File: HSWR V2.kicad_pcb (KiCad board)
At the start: 4 copper layers, 152 x 139 mm, 156 parts, among them IC1 INA181, IC2 INA181, IC3 INA181, IC4 ADUM3054, IC5 ADuM4160, IC6 JW5052C, IC7 JW5052C, IC8 B1212S-2W, J1 IO, J10 SWD, J4 USB_B, J5 B+, J6 B-, J7 U, J8 V, J9 W, Q11 IXFK300N20X3, Q12 IXFK300N20X3, Q3 IXFK300N20X3, Q4 IXFK300N20X3, Q7 IXFK300N20X3, Q8 IXFK300N20X3, U1 STM32F405RGTx, U2 IRS2186, U3 IRS2186, U4 IRS2186, U5 AP1117-50, Y1 8MHz

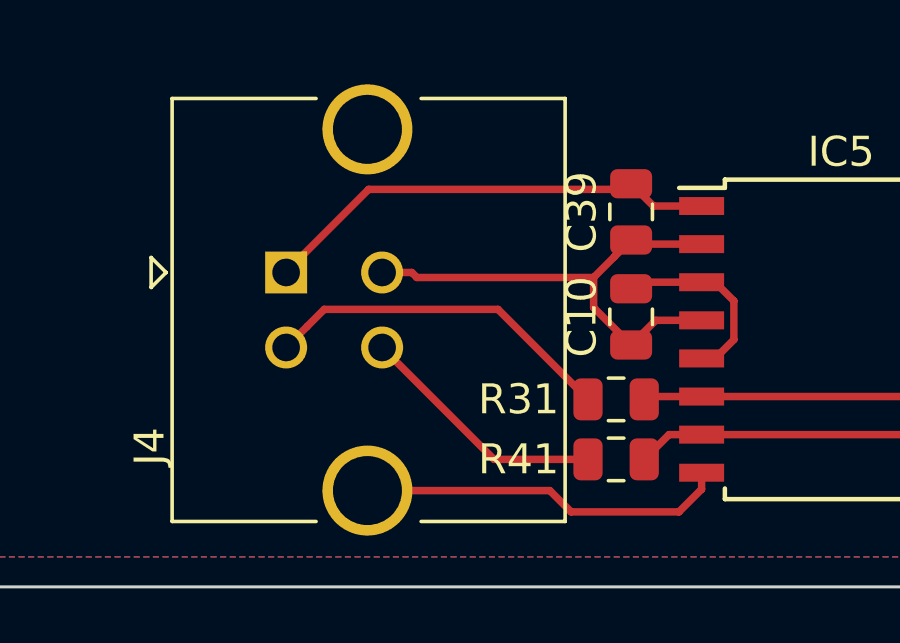
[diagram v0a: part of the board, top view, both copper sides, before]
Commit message: - corrected current filter resistors - adapted USB footprint - added 0.1% note to dc bus voltage divider
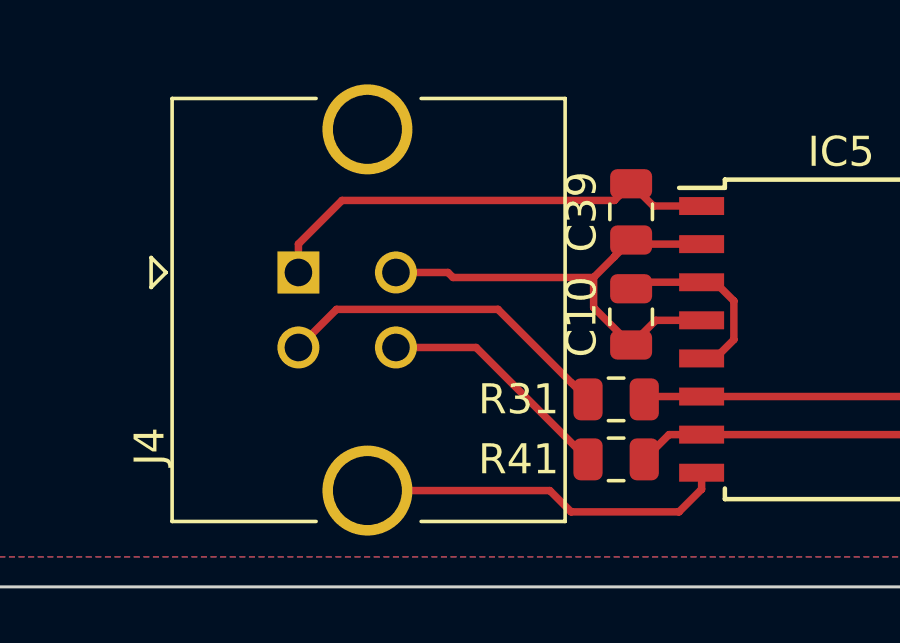
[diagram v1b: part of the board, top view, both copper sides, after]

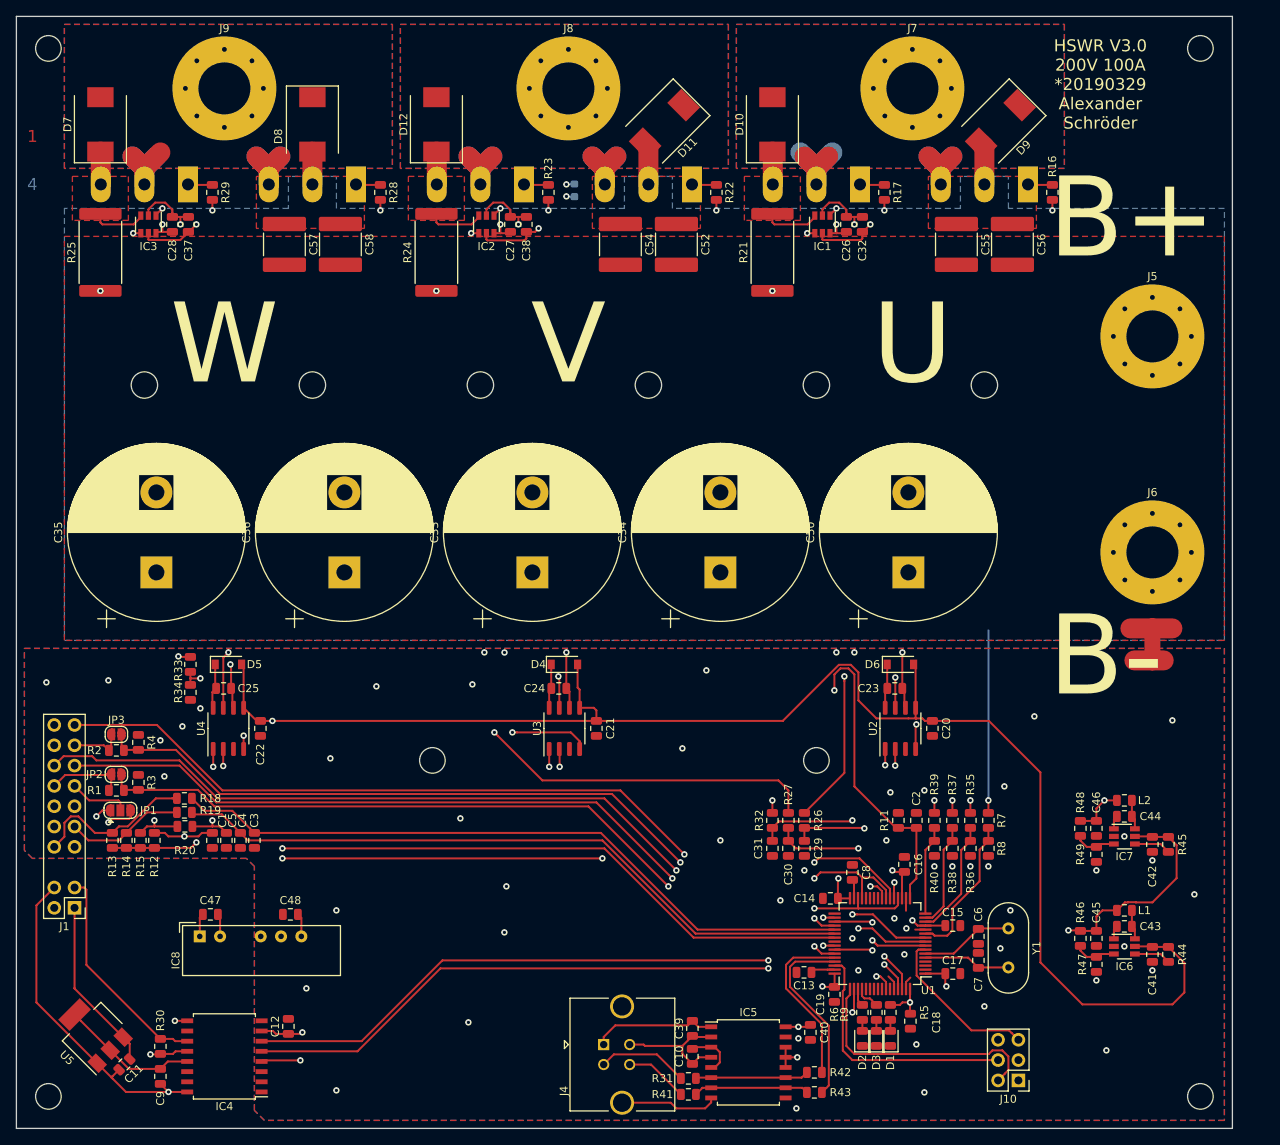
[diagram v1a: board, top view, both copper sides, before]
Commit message: - rescued schematic - added *.sch-bak to ignore - fixed bypass diode polarity - fixed PDEN being low - added 0R resistors instead of USB iso option - added caps to DCDC - added filter to VDDA
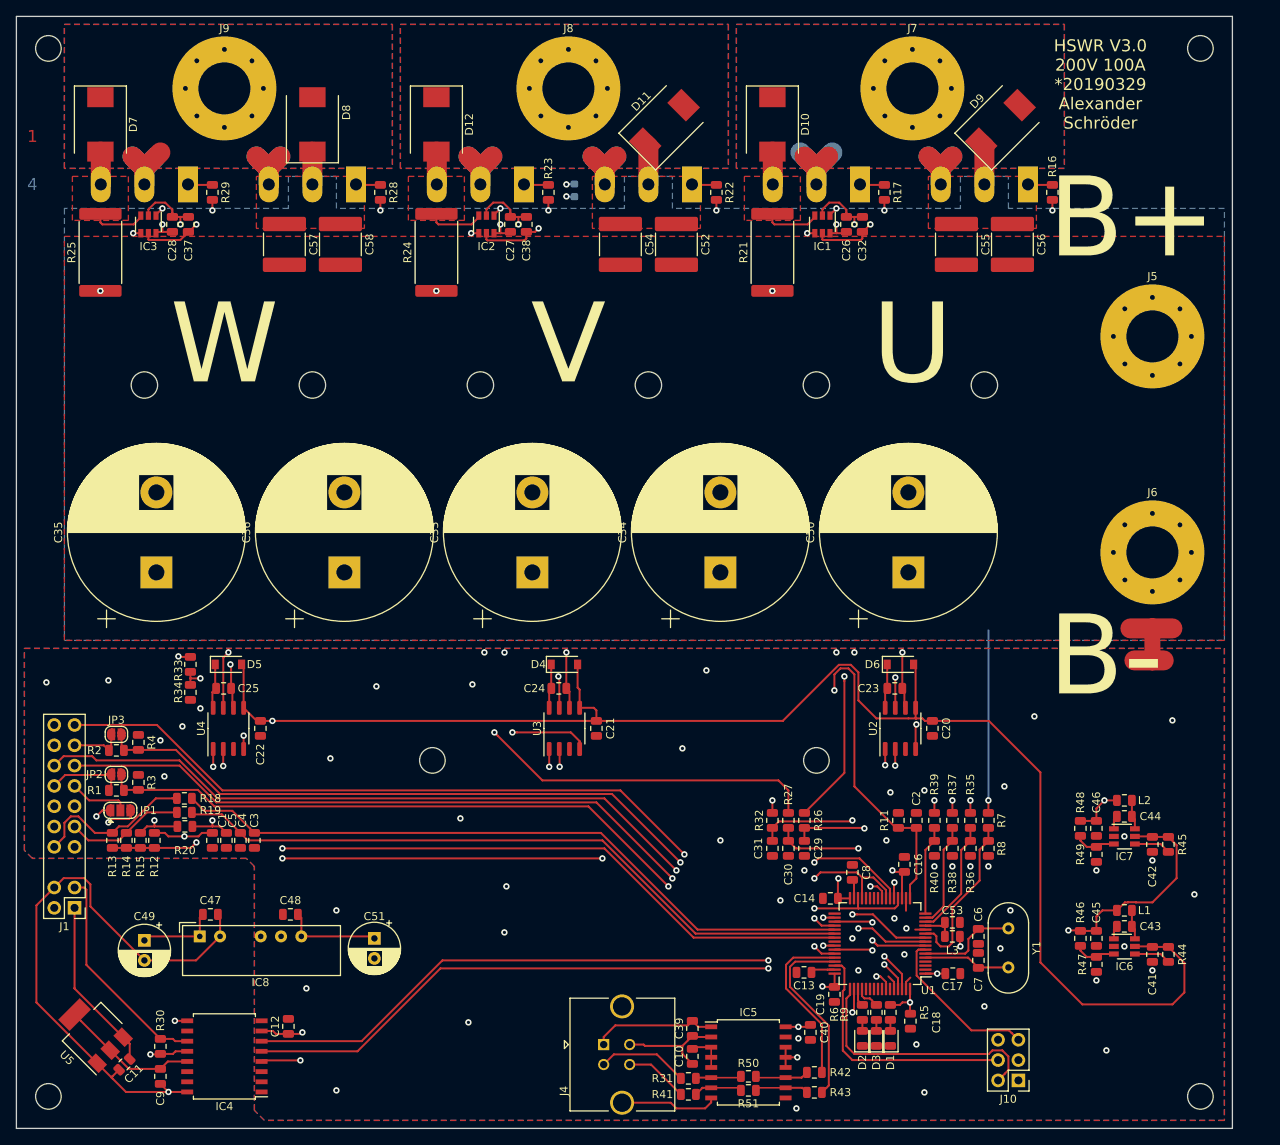
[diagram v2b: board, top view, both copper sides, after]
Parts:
- removed C15: 1u, Capacitor_SMD:C_0805_2012Metric
- added C49: 100u/16V, Capacitor_THT:CP_Radial_D6.3mm_P2.50mm, F.Cu at (83.0, 139.5)
- added C51: 100u/16V, Capacitor_THT:CP_Radial_D6.3mm_P2.50mm, F.Cu at (111.8, 139.2)
- added C53: 22u/6V3, Capacitor_SMD:C_0805_2012Metric, F.Cu at (184.0, 137.2)
- added L3: 22uH, Inductor_SMD:L_0805_2012Metric, F.Cu at (184.0, 139.0)
- added R50: 0R, Resistor_SMD:R_0805_2012Metric, F.Cu at (158.5, 156.5)
- added R51: 0R, Resistor_SMD:R_0805_2012Metric, F.Cu at (158.5, 158.2)
- C41: value 22u -> 22u/16V
- C42, C45, C46: value 22u -> 22u/6V3
- R26, R27, R32: value 470R -> 100R
- R7: value 300k -> 300k 0.1%
- R8: value 4k7 -> 4k7 0.1%
- turned D10 to 270 degrees
- turned D11 to 45 degrees
- turned D12 to 270 degrees
- turned D7 to 270 degrees
- turned D8 to 90 degrees
- turned D9 to 45 degrees
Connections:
- D10 pad 1: /Mosfet driver/U_VS -> /Power MOSFETS/U
- D10 pad 2: /Power MOSFETS/U -> /Mosfet driver/U_VS
- D11 pad 1: /Power MOSFETS/V -> +BATT
- D11 pad 2: +BATT -> /Power MOSFETS/V
- D12 pad 1: /Mosfet driver/V_VS -> /Power MOSFETS/V
- D12 pad 2: /Power MOSFETS/V -> /Mosfet driver/V_VS
- D7 pad 1: /Mosfet driver/W_VS -> /Power MOSFETS/W
- D7 pad 2: /Power MOSFETS/W -> /Mosfet driver/W_VS
- D8 pad 1: /Power MOSFETS/W -> +BATT
- D8 pad 2: +BATT -> /Power MOSFETS/W
- D9 pad 1: /Power MOSFETS/U -> +BATT
- D9 pad 2: +BATT -> /Power MOSFETS/U
- IC5 pad 4: GNDD -> Net-(C10-Pad2)
- IC5 pad 6: Net-(IC5-Pad11) -> Net-(IC5-Pad6)
- IC5 pad 7: Net-(IC5-Pad10) -> Net-(IC5-Pad7)
- R31 pad 1: Net-(IC5-Pad11) -> Net-(IC5-Pad6)
- R41 pad 2: Net-(IC5-Pad10) -> Net-(IC5-Pad7)
- U1 pad 13: +3V3 -> Net-(C53-Pad2)
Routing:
- net (no net): track 571.9 -> 0.00 mm
- net +12V: track 219.0 -> 228.2 mm
- net Net-(IC5-Pad10): track 14.5 -> 6.75 mm
- net Net-(IC5-Pad11): track 14.2 -> 6.71 mm
- net Net-(IC5-Pad7): track 0.00 -> 6.10 mm
- net Net-(IC5-Pad6): track 0.00 -> 5.73 mm
- net Earth: track 78.4 -> 83.5 mm
- net +3V3: track 246.8 -> 242.0 mm
- net Net-(C53-Pad2): track 0.00 -> 4.37 mm
- net GNDD: track 42.9 -> 40.2 mm
- net /MCU/BUS_U: track 18.4 -> 20.9 mm
- net Net-(C10-Pad2): track 6.40 -> 4.98 mm
- net /MCU/CAN_VSS_SENSE: track 84.8 -> 83.4 mm
- net +12VA: track 41.9 -> 42.9 mm
- net Net-(C6-Pad2): track 11.7 -> 12.5 mm

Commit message: - changed CSA for Hall effect sensors - updated power stage layout
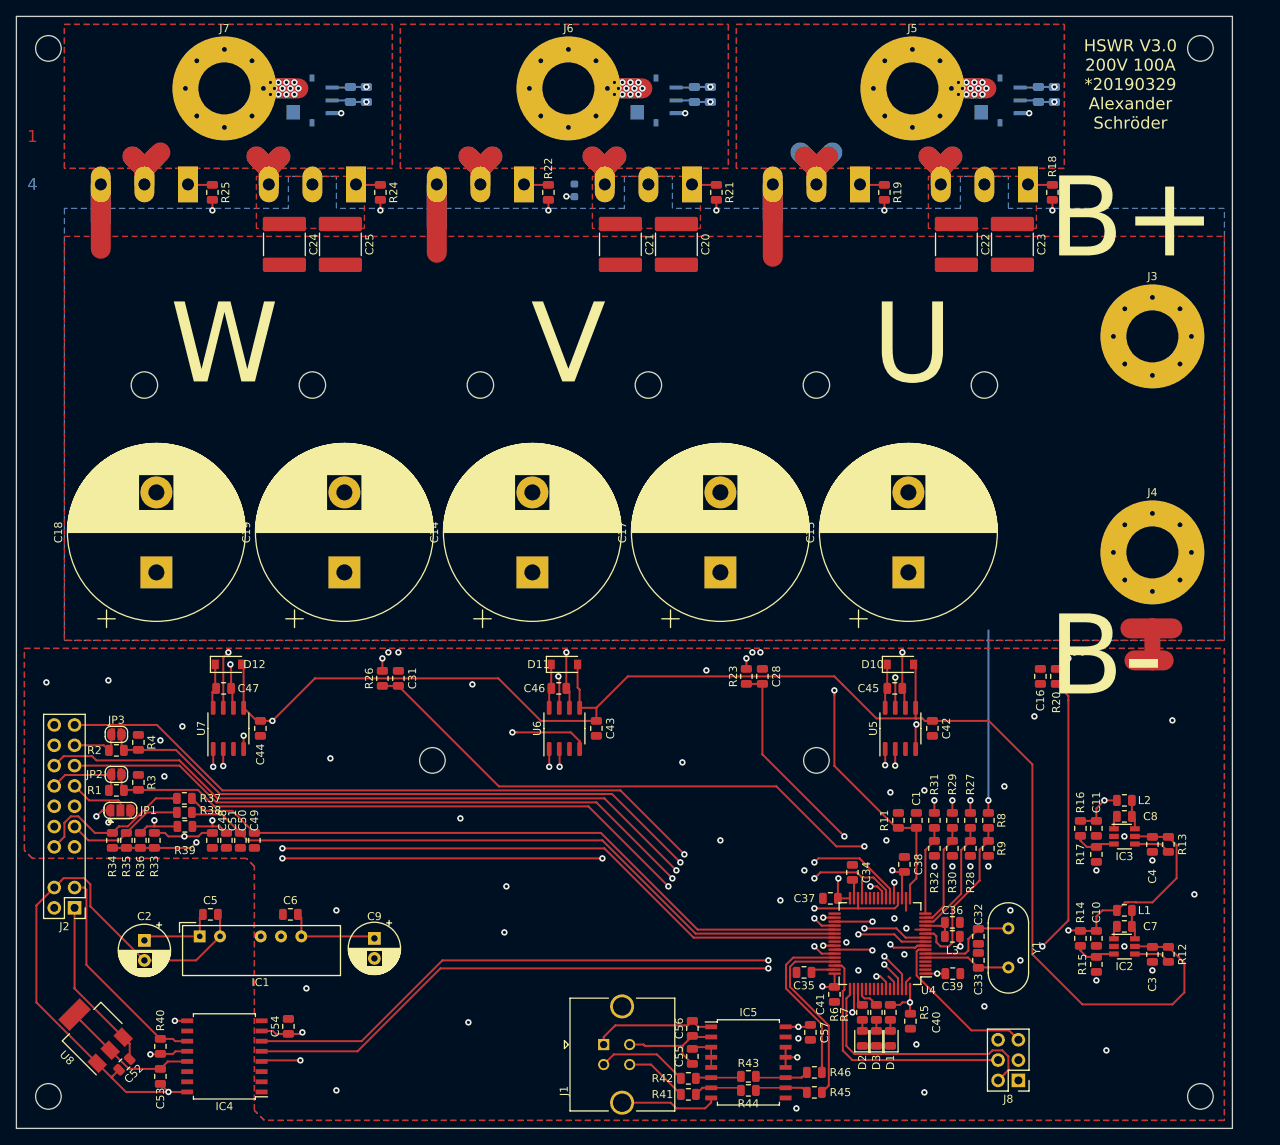
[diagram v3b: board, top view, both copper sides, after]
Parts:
- removed the C32 at (172.8, 50.0)
- removed the C37 at (88.5, 50.0)
- removed the C38 at (130.8, 50.0)
- removed the D10 at (161.5, 37.5)
- removed the D11 at (148.0, 37.5)
- removed the D12 at (119.5, 37.5)
- removed D7, D8, D9: FR6J-TP, Diode_SMD:D_SMC
- removed the IC1 at (167.8, 50.0)
- removed the IC2 at (125.8, 50.0)
- removed the IC3 at (83.5, 50.0)
- removed the R21 at (161.5, 53.5)
- removed the R24 at (119.5, 53.5)
- removed the R25 at (77.5, 53.5)
- removed the R27 at (163.5, 124.5)
- removed the R32 at (161.5, 124.5)
- removed the R33 at (88.8, 105.0)
- removed the R34 at (88.8, 108.5)
- added C12: 100n, Capacitor_SMD:C_0805_2012Metric, B.Cu at (194.8, 33.8)
- added C13: 1u, Capacitor_SMD:C_0805_2012Metric, B.Cu at (196.8, 33.8)
- added C16: 4n7, Capacitor_SMD:C_0805_2012Metric, F.Cu at (195.0, 106.5)
- added R20: 1k, Resistor_SMD:R_0805_2012Metric, F.Cu at (197.0, 106.5)
- added R23: 1k, Resistor_SMD:R_0805_2012Metric, F.Cu at (158.2, 106.5)
- added U1: ACS781xLRTR-150B, Sensor_Current:Allegro_PSOF-7_4.8x6.4mm_P1.60mm, B.Cu at (190.0, 34.5)
- added U2: ACS781xLRTR-150B, Sensor_Current:Allegro_PSOF-7_4.8x6.4mm_P1.60mm, B.Cu at (147.0, 34.5)
- added U3: ACS781xLRTR-150B, Sensor_Current:Allegro_PSOF-7_4.8x6.4mm_P1.60mm, B.Cu at (104.0, 34.5)
- C26: value 1u -> 100n; moved to B.Cu
- C27: moved to B.Cu
- C28: value 1u -> 4n7
- C29: value 4n7 -> 100n; moved to B.Cu
- C30: value 4n7 -> 1u; moved to B.Cu
- R26: value 100R -> 1k
- moved C29 110.0 mm to (108.8, 33.8)
- moved C30 108.0 mm to (110.8, 33.8), turned to 90 degrees
- moved C28 92.9 mm to (160.2, 106.5), turned to 90 degrees
- moved R26 55.7 mm to (112.8, 106.8)
- moved C31 51.4 mm to (114.8, 106.8), turned to 90 degrees
- moved C27 29.8 mm to (153.8, 33.8), turned to 90 degrees
- moved C26 25.0 mm to (151.8, 33.8)
- renumbered C2 to C1, C45 to C10, C46 to C11, C33 to C14, C50 to C15, C34 to C17, C35 to C18, C36 to C19, C49 to C2, C52 to C20, C54 to C21, C55 to C22, C56 to C23, C57 to C24, C58 to C25, C41 to C3, C6 to C32, C7 to C33, C8 to C34, C13 to C35, C53 to C36, C14 to C37, C16 to C38, C17 to C39, C42 to C4, C18 to C40, C19 to C41, C20 to C42, C21 to C43, C22 to C44, C23 to C45, C24 to C46, C25 to C47, C1 to C48, C3 to C49, C47 to C5, C4 to C50, C5 to C51, C11 to C52, C9 to C53, C12 to C54, C10 to C55, C39 to C56, C40 to C57, C48 to C6, C43 to C7, C44 to C8, C51 to C9, D6 to D10, D4 to D11, D5 to D12, IC8 to IC1, IC6 to IC2, IC7 to IC3, J4 to J1, J1 to J2, J5 to J3, J6 to J4, J7 to J5, J8 to J6, J9 to J7, J10 to J8, Q3 to Q1, Q4 to Q2, Q7 to Q3, Q8 to Q4, Q11 to Q5, Q12 to Q6, R44 to R12, R45 to R13, R46 to R14, R47 to R15, R48 to R16, R49 to R17, R16 to R18, R17 to R19, R22 to R21, R23 to R22, R28 to R24, R29 to R25, R35 to R27, R36 to R28, R37 to R29, R38 to R30, R39 to R31, R40 to R32, R12 to R33, R13 to R34, R14 to R35, R15 to R36, R18 to R37, R19 to R38, R20 to R39, R30 to R40, R31 to R42, R50 to R43, R51 to R44, R43 to R45, R42 to R46, R9 to R7, R7 to R8, R8 to R9, U1 to U4, U2 to U5, U3 to U6, U4 to U7, U5 to U8
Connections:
- C26 pad 1: GND -> +3V3
- C26 pad 2: +3V3 -> GND
- C28 pad 1: GND -> /MCU/V_I
- C28 pad 2: +3V3 -> GND
- C29 pad 1: /MCU/U_I -> +3V3
- C30 pad 1: /MCU/V_I -> GND
- C30 pad 2: GND -> +3V3
- C45 pad 2: /Power MOSFETS/U -> /Mosfet driver/U_VP
- C46 pad 2: /Power MOSFETS/V -> /Mosfet driver/V_VP
- C47 pad 2: /Power MOSFETS/W -> /Mosfet driver/W_VP
- Q1 pad 3: /Power MOSFETS/U -> /Mosfet driver/U_VP
- Q2 pad 2: /Power MOSFETS/U -> /Mosfet driver/U_VP
- Q2 pad 3: /Mosfet driver/U_VS -> GNDPWR
- Q3 pad 3: /Power MOSFETS/V -> /Mosfet driver/V_VP
- Q4 pad 2: /Power MOSFETS/V -> /Mosfet driver/V_VP
- Q4 pad 3: /Mosfet driver/V_VS -> GNDPWR
- Q5 pad 3: /Power MOSFETS/W -> /Mosfet driver/W_VP
- Q6 pad 2: /Power MOSFETS/W -> /Mosfet driver/W_VP
- Q6 pad 3: /Mosfet driver/W_VS -> GNDPWR
- R26 pad 1: /MCU/U_I -> /MCU/W_I
- R27 pad 1: /Power MOSFETS/U -> /Mosfet driver/U_VP
- R29 pad 1: /Power MOSFETS/V -> /Mosfet driver/V_VP
- R31 pad 1: /Power MOSFETS/W -> /Mosfet driver/W_VP
- U5 pad 6: /Power MOSFETS/U -> /Mosfet driver/U_VP
- U6 pad 6: /Power MOSFETS/V -> /Mosfet driver/V_VP
- U7 pad 6: /Power MOSFETS/W -> /Mosfet driver/W_VP
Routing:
- net /Mosfet driver/W_VP: track 0.00 -> 200.4 mm, vias 0 -> 2
- net U2_REF: track 170.9 -> 0.00 mm, vias 4 -> 0
- net /Power MOSFETS/W: track 201.0 -> 36.3 mm, vias 2 -> 12
- net /Mosfet driver/V_VP: track 0.00 -> 162.0 mm, vias 0 -> 2
- net Net-(IC3-Pad1): track 144.8 -> 0.00 mm, vias 2 -> 0
- net /Power MOSFETS/V: track 162.0 -> 36.3 mm, vias 2 -> 12
- net /Mosfet driver/U_VP: track 0.00 -> 123.0 mm, vias 0 -> 2
- net Net-(IC2-Pad1): track 110.4 -> 0.00 mm, vias 2 -> 0
- net /Power MOSFETS/U: track 123.0 -> 36.3 mm, vias 2 -> 12
- net Net-(R23-Pad2): track 0.00 -> 76.6 mm, vias 0 -> 2
- net Net-(R20-Pad2): track 0.00 -> 75.9 mm, vias 0 -> 2
- net /MCU/W_I: track 34.1 -> 86.9 mm
- net +3V3: track 242.0 -> 289.1 mm, vias 19 -> 18
- net GND: track 204.3 -> 238.3 mm, vias 56 -> 55
- net /MCU/U_I: track 30.5 -> 58.9 mm
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- added copper zone on B.Cu, net /Mosfet driver/U_VP
- added copper zone on F.Cu, net /Mosfet driver/U_VP
- added copper zone on GND, net /Mosfet driver/U_VP
- added copper zone on Power1, net /Mosfet driver/U_VP
- added copper zone on B.Cu, net /Mosfet driver/V_VP
- added copper zone on F.Cu, net /Mosfet driver/V_VP
- added copper zone on GND, net /Mosfet driver/V_VP
- added copper zone on Power1, net /Mosfet driver/V_VP
- added copper zone on B.Cu, net /Mosfet driver/W_VP
- added copper zone on F.Cu, net /Mosfet driver/W_VP
- added copper zone on GND, net /Mosfet driver/W_VP
- added copper zone on Power1, net /Mosfet driver/W_VP
- removed copper zone on F.Cu, net /Mosfet driver/U_VS
- removed copper zone on F.Cu, net /Mosfet driver/V_VS
- removed copper zone on F.Cu, net /Mosfet driver/W_VS
- removed copper zone on B.Cu, net /Power MOSFETS/U
- removed copper zone on F.Cu, net /Power MOSFETS/U
- removed copper zone on GND, net /Power MOSFETS/U
- removed copper zone on Power1, net /Power MOSFETS/U
- removed copper zone on B.Cu, net /Power MOSFETS/V
- removed copper zone on F.Cu, net /Power MOSFETS/V
- removed copper zone on GND, net /Power MOSFETS/V
- removed copper zone on Power1, net /Power MOSFETS/V
- removed copper zone on B.Cu, net /Power MOSFETS/W
- removed copper zone on F.Cu, net /Power MOSFETS/W
- removed copper zone on GND, net /Power MOSFETS/W
- removed copper zone on Power1, net /Power MOSFETS/W
